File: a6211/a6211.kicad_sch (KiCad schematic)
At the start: 27 parts, among them J1 Conn_01x02, J2 Conn_01x02, J3 Conn_01x07, J4 Conn_01x05, J5 Conn_01x02, U1 A6211

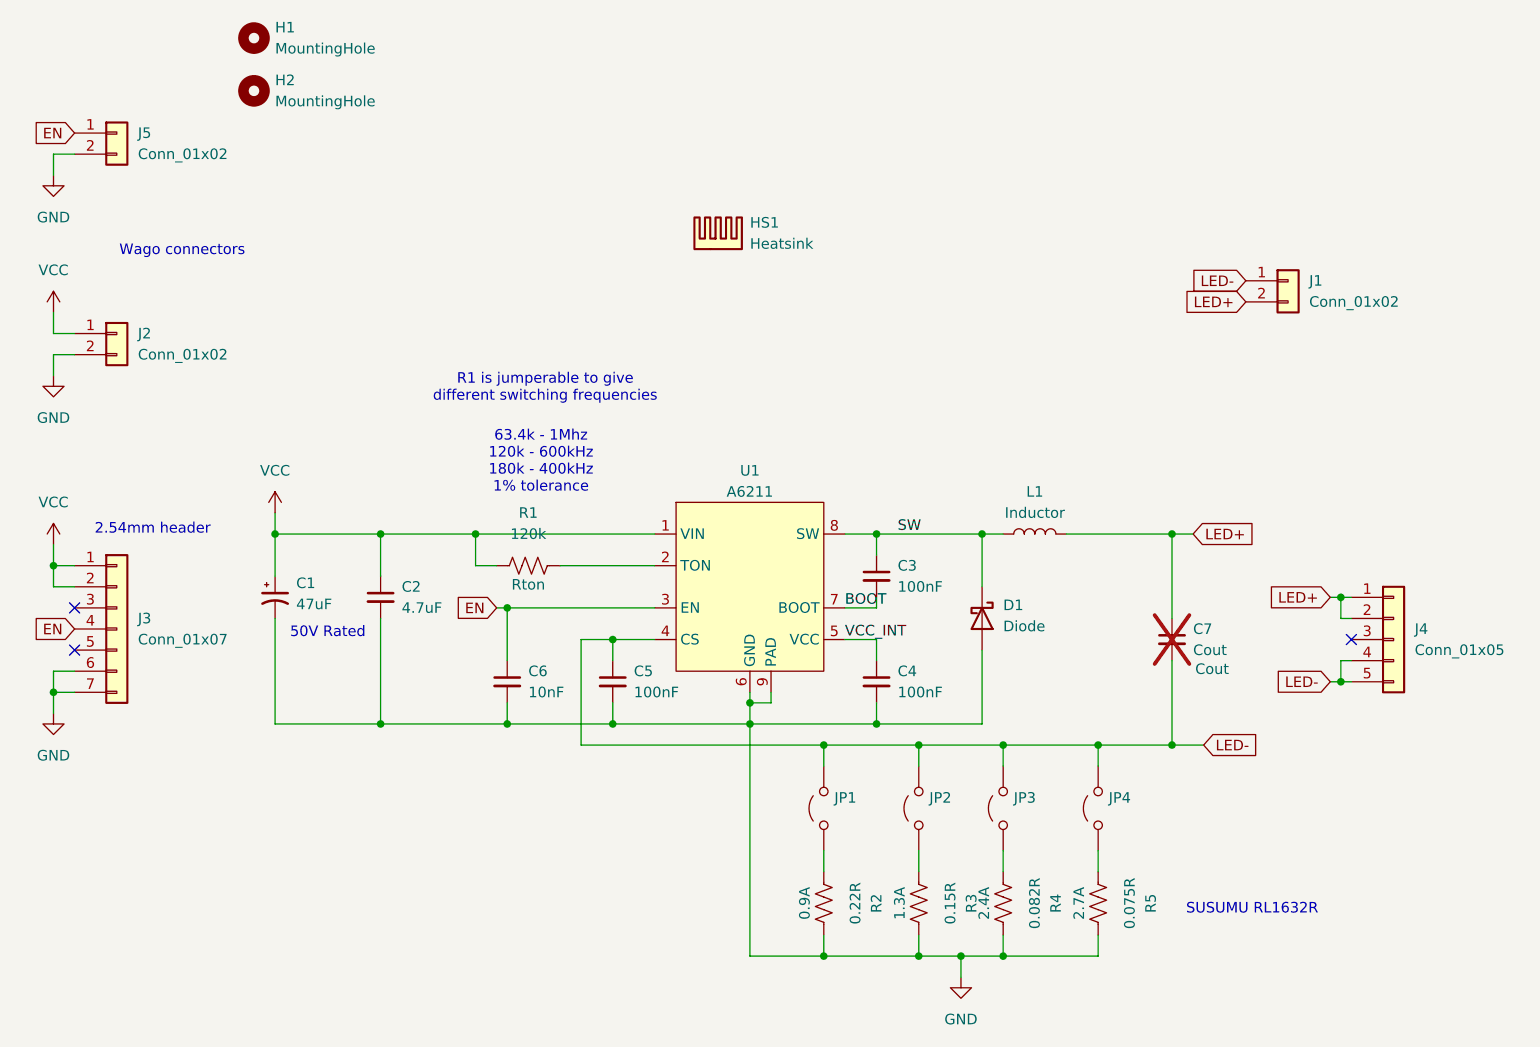
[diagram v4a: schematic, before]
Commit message: A6211 JLCPCB reference
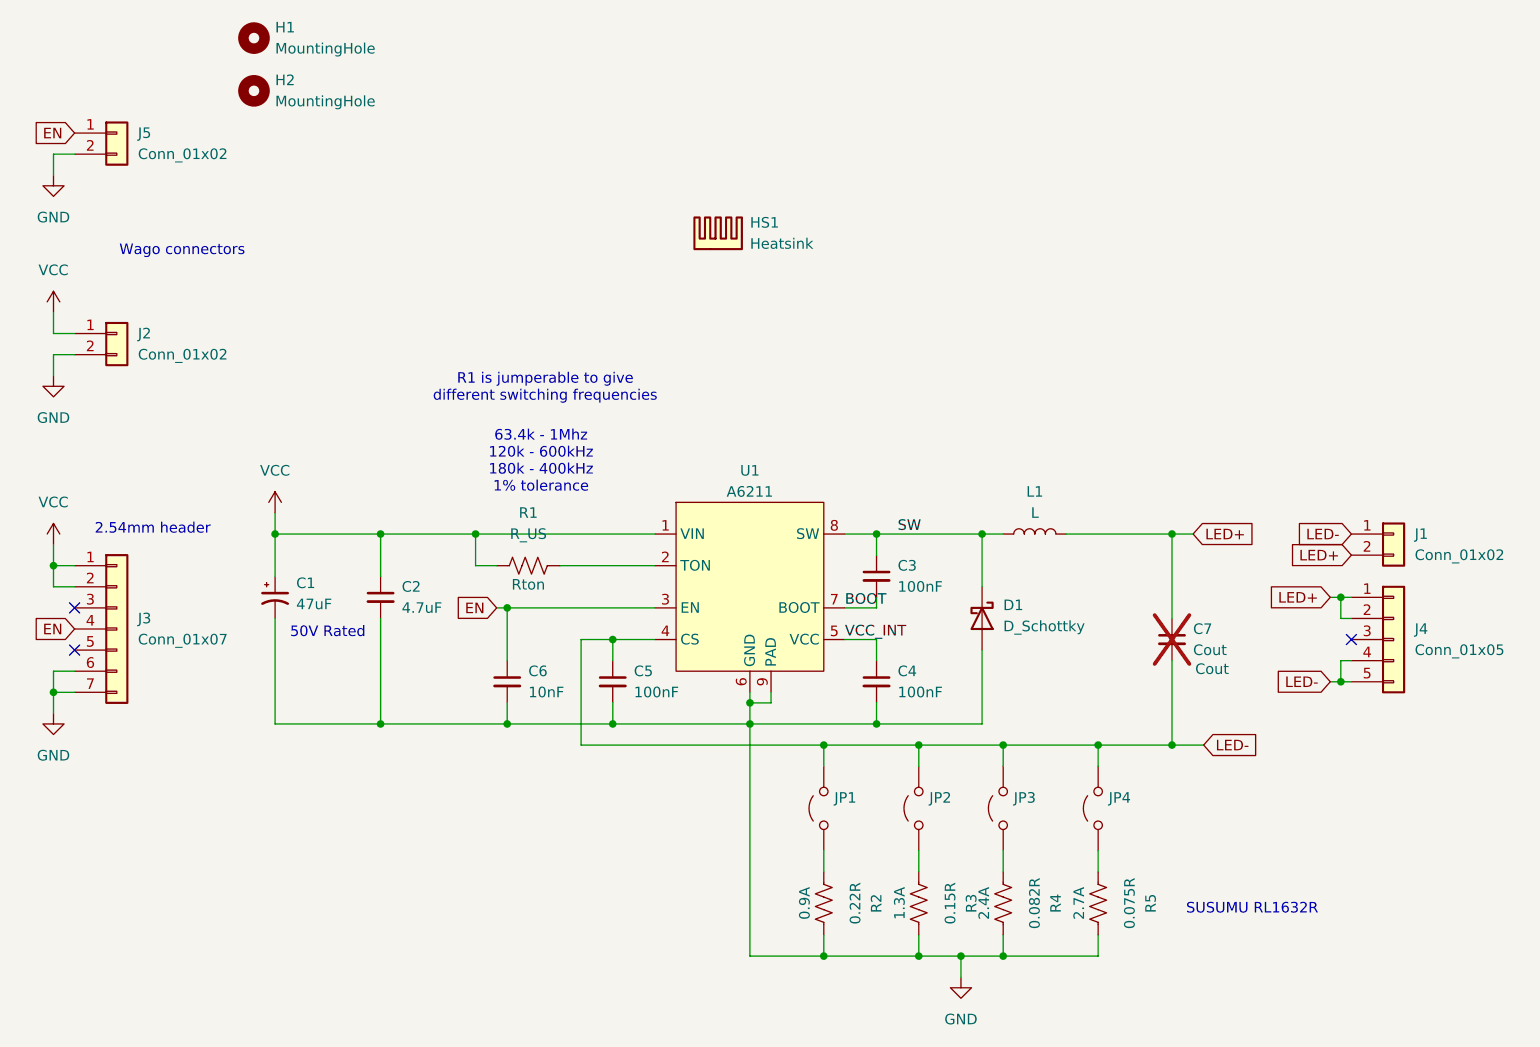
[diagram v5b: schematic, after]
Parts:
- D1: value Diode -> D_Schottky
- L1: value Inductor -> L
- R1: value 120k -> R_US
- U1: LCSC (none) -> C150827
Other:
- moved on the sheet: J1
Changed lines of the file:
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@@
 	(global_label "LED-"
 		(shape input)
-		(at 181.61 57.15 180)
+		(at 194.31 87.63 180)
 		(fields_autoplaced yes)
 		(effects
@@
 		)
 		(property "Intersheetrefs" "${INTERSHEET_REFS}"
-			(at 173.6053 57.15 0)
+			(at 186.3053 87.63 0)
 			(effects
 				(font
@@
 	(global_label "LED+"
 		(shape input)
-		(at 181.61 59.69 180)
+		(at 194.31 90.17 180)
 		(fields_autoplaced yes)
 		(effects
@@
 		)
 		(property "Intersheetrefs" "${INTERSHEET_REFS}"
-			(at 173.6053 59.69 0)
+			(at 186.3053 90.17 0)
 			(effects
 				(font
@@
 		)
 		(instances
-			(project ""
+			(project "a6211"
 				(path "/0eae7fad-4295-4de1-8a09-6528fc5757a4"
 					(reference "JP1")
@@
 			)
 		)
+		(property "LCSC" "C150827"
+			(at 121.92 93.98 0)
+			(effects
+				(font
+					(size 1.27 1.27)
+				)
+				(hide yes)
+			)
+		)
 		(pin "4"
 		)
@@
 		)
 		(instances
-			(project ""
+			(project "a6211"
 				(path "/0eae7fad-4295-4de1-8a09-6528fc5757a4"
 					(reference "U1")
@@
 		)
 		(instances
-			(project ""
+			(project "a6211"
 				(path "/0eae7fad-4295-4de1-8a09-6528fc5757a4"
 					(reference "#PWR02")
@@
 		)
 		(instances
-			(project ""
+			(project "a6211"
 				(path "/0eae7fad-4295-4de1-8a09-6528fc5757a4"
 					(reference "C1")
@@
 		)
 		(instances
-			(project ""
+			(project "a6211"
 				(path "/0eae7fad-4295-4de1-8a09-6528fc5757a4"
 					(reference "J2")
@@
 		)
 		(instances
-			(project ""
+			(project "a6211"
 				(path "/0eae7fad-4295-4de1-8a09-6528fc5757a4"
 					(reference "J3")
@@
 		)
 		(instances
-			(project ""
+			(project "a6211"
 				(path "/0eae7fad-4295-4de1-8a09-6528fc5757a4"
 					(reference "H1")
@@
 			)
 		)
-		(property "Value" "Inductor"
+		(property "Value" "L"
 			(at 156.21 85.09 90)
 			(effects
@@
 		)
 		(instances
-			(project ""
+			(project "a6211"
 				(path "/0eae7fad-4295-4de1-8a09-6528fc5757a4"
 					(reference "L1")
@@
 			)
 		)
-		(property "Value" "120k"
+		(property "Value" "R_US"
 			(at 95.25 87.63 90)
 			(effects
@@
 		)
 		(instances
-			(project ""
+			(project "a6211"
 				(path "/0eae7fad-4295-4de1-8a09-6528fc5757a4"
 					(reference "R1")
@@
 	(symbol
 		(lib_id "Connector_Generic:Conn_01x02")
-		(at 186.69 57.15 0)
+		(at 199.39 87.63 0)
 		(unit 1)
 		(exclude_from_sim no)
@@
 		(fields_autoplaced yes)
 		(property "Reference" "J1"
-			(at 189.23 57.1499 0)
+			(at 201.93 87.6299 0)
 			(effects
 				(font
@@
 		)
 		(property "Value" "Conn_01x02"
-			(at 189.23 59.6899 0)
+			(at 201.93 90.1699 0)
 			(effects
 				(font
@@
 		)
 		(property "Footprint" "MHCI:2060-452-998-404 Wago"
-			(at 186.69 57.15 0)
+			(at 199.39 87.63 0)
 			(effects
 				(font
@@
 		)
 		(property "Datasheet" "~"
-			(at 186.69 57.15 0)
+			(at 199.39 87.63 0)
 			(effects
 				(font
@@
 		)
 		(property "Description" "Generic connector, single row, 01x02, script generated (kicad-library-utils/schlib/autogen/connector/)"
-			(at 186.69 57.15 0)
+			(at 199.39 87.63 0)
 			(effects
 				(font
@@
 		)
 		(property "MFR" "2060-452/998-404"
-			(at 186.69 57.15 0)
+			(at 199.39 87.63 0)
 			(effects
 				(font
@@
 		)
 		(instances
-			(project ""
+			(project "a6211"
 				(path "/0eae7fad-4295-4de1-8a09-6528fc5757a4"
 					(reference "J1")
@@
 		)
 		(instances
-			(project ""
+			(project "a6211"
 				(path "/0eae7fad-4295-4de1-8a09-6528fc5757a4"
 					(reference "J4")
@@
 		)
 		(instances
-			(project ""
+			(project "a6211"
 				(path "/0eae7fad-4295-4de1-8a09-6528fc5757a4"
 					(reference "C7")
@@
 		)
 		(instances
-			(project ""
+			(project "a6211"
 				(path "/0eae7fad-4295-4de1-8a09-6528fc5757a4"
 					(reference "HS1")
@@
 			)
 		)
-		(property "Value" "Diode"
+		(property "Value" "D_Schottky"
 			(at 152.4 98.7424 90)
 			(effects
@@
 		)
 		(instances
-			(project ""
+			(project "a6211"
 				(path "/0eae7fad-4295-4de1-8a09-6528fc5757a4"
 					(reference "D1")

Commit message: A6211 v1.1
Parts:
- removed JP1, JP2, JP3, JP4: ~, Jumper:SolderJumper-2_P1.3mm_Open_RoundedPad1.0x1.5mm, symbol Jumper:Jumper_2_Open
- removed R4: 0.082R, Resistor_SMD:R_1206_3216Metric, symbol Device:R_US
- removed R5: 0.075R, Resistor_SMD:R_1206_3216Metric, symbol Device:R_US
- added C8: 470nF, Capacitor_SMD:C_1206_3216Metric, symbol Device:C_Small
- added JP1: Jumper_3_Open, Jumper:SolderJumper-3_P1.3mm_Open_RoundedPad1.0x1.5mm_NumberLabels, symbol Jumper:Jumper_3_Open
- C1: LCSC (none) -> C40078
- C2: LCSC (none) -> C29823
- C3: value 100nF -> 47nF; LCSC (none) -> C1622
- C4, C5: LCSC (none) -> C14663
- C6: LCSC (none) -> C57112
- C7: value Cout -> 2.2uF; footprint Capacitor_SMD:C_0603_1608Metric_Pad1.08x0.95mm_HandSolder -> Capacitor_SMD:C_1206_3216Metric; LCSC (none) -> C50254; now fitted
- D1: LCSC (none) -> C7436542; MFR B560C-13-F -> (none)
- L1: value L -> 10uH; footprint Inductor_SMD:L_10.4x10.4_H4.8 -> Inductor_SMD:L_Coilcraft_XAL6060-XXX; LCSC (none) -> C5119929; MFR B82464G4103M -> (none)
- R1: LCSC (none) -> C23231; now not fitted; now left out of the parts list
- R2: value 0.22R -> 120k; footprint Resistor_SMD:R_1206_3216Metric -> Resistor_SMD:R_0603_1608Metric_Pad0.98x0.95mm_HandSolder; LCSC (none) -> C25808; MFR RL1632R-R220-F -> (none)
- R3: LCSC (none) -> C2683383
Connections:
- net GND: no longer R2.2
- net LED+: now also C8.1
- net LED-: now also R3.1, JP1.2 (C); no longer C7.2
- net VCC: now also R2.1; no longer R1.1
- net at R1.2: no longer U1.2 (TON)
- new net: R2.2, U1.2 (TON)
- new net: C7.2, JP1.3 (B)
- new net: C8.2, JP1.1 (A)

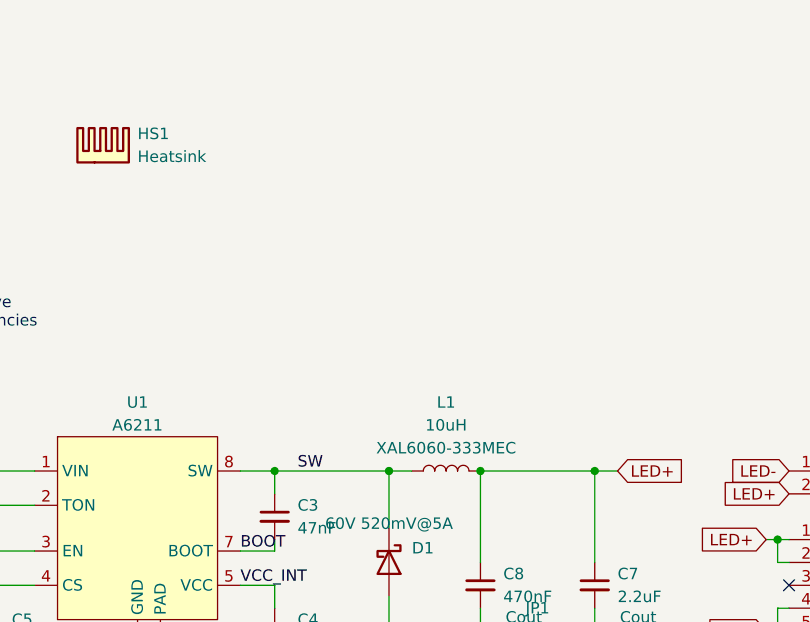
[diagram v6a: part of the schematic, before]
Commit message: A6211 - cheaper inductor
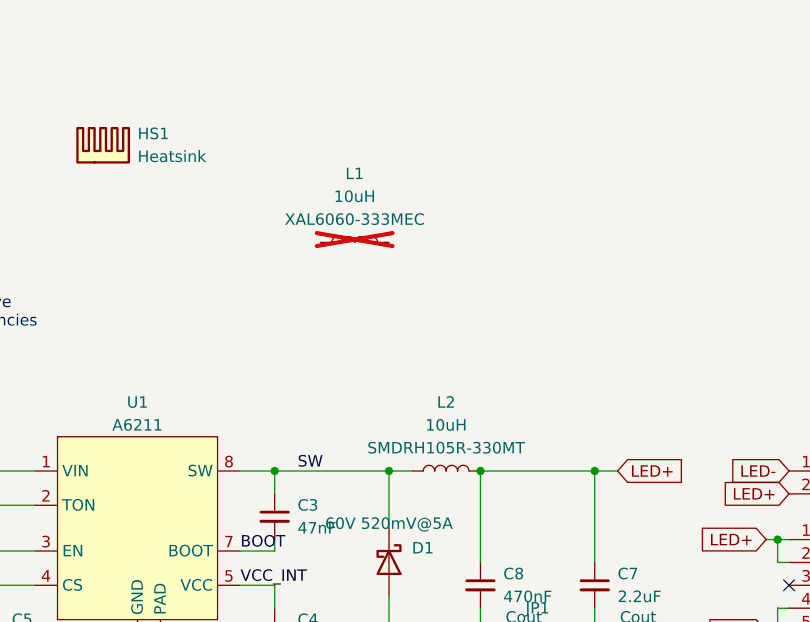
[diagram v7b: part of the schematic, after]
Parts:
- added L2: 10uH, Inductor_SMD:L_10.4x10.4_H4.8, symbol Device:L
- C8: footprint Capacitor_SMD:C_1206_3216Metric -> Capacitor_SMD:C_0805_2012Metric; LCSC C50254 -> C13967
- L1: now not fitted; now left out of the parts list
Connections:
- net LED+: now also L2.2; no longer L1.2
- net SW: now also L2.1; no longer L1.1
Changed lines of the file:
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@@
 	)
 	(junction
-		(at 160.02 87.63)
-		(diameter 0)
-		(color 0 0 0 0)
-	)
-	(junction
 		(at 121.92 110.49)
 		(diameter 0)
@@
 	)
 	(junction
+		(at 160.02 87.63)
+		(diameter 0)
+		(color 0 0 0 0)
+	)
+	(junction
 		(at 166.37 113.03)
 		(diameter 0)
@@
 	)
 	(symbol
+		(lib_id "Device:L")
+		(at 156.21 87.63 90)
+		(unit 1)
+		(exclude_from_sim no)
+		(in_bom yes)
+		(on_board yes)
+		(dnp no)
+		(fields_autoplaced yes)
+		(property "Reference" "L2"
+			(at 156.21 80.01 90)
+			(effects
+				(font
+					(size 1.27 1.27)
+				)
+			)
+		)
+		(property "Value" "10uH"
+			(at 156.21 82.55 90)
+			(effects
+				(font
+					(size 1.27 1.27)
+				)
+			)
+		)
+		(property "Footprint" "Inductor_SMD:L_10.4x10.4_H4.8"
+			(at 156.21 87.63 0)
+			(effects
+				(font
+					(size 1.27 1.27)
+				)
+				(hide yes)
+			)
+		)
+		(property "Datasheet" "~"
+			(at 156.21 87.63 0)
+			(effects
+				(font
+					(size 1.27 1.27)
+				)
+				(hide yes)
+			)
+		)
+		(property "Description" "SMDRH105R-330MT"
+			(at 156.21 85.09 90)
+			(effects
+				(font
+					(size 1.27 1.27)
+				)
+			)
+		)
+		(property "LCSC" "C9186"
+			(at 156.21 87.63 90)
+			(effects
+				(font
+					(size 1.27 1.27)
+				)
+				(hide yes)
+			)
+		)
+		(pin "1"
+		)
+		(pin "2"
+		)
+		(instances
+			(project "a6211"
+				(path "/0eae7fad-4295-4de1-8a09-6528fc5757a4"
+					(reference "L2")
+					(unit 1)
+				)
+			)
+		)
+	)
+	(symbol
 		(lib_id "A6211:A6211")
 		(at 121.92 93.98 0)
@@
 			)
 		)
-		(property "Footprint" "Capacitor_SMD:C_1206_3216Metric"
+		(property "Footprint" "Capacitor_SMD:C_0805_2012Metric"
 			(at 160.02 100.33 0)
 			(effects
@@
 			)
 		)
-		(property "LCSC" "C50254"
+		(property "LCSC" "C13967"
 			(at 160.02 100.33 0)
 			(effects
@@
 	)
 	(symbol
-		(lib_id "power:GND")
-		(at 38.1 44.45 0)
+		(lib_id "Device:L")
+		(at 146.05 62.23 90)
 		(unit 1)
-		(exclude_from_sim no)
-		(in_bom yes)
-		(on_board yes)
-		(dnp no)
+		(exclude_from_sim yes)
+		(in_bom no)
+		(on_board no)
+		(dnp yes)
 		(fields_autoplaced yes)
-		(property "Reference" "#PWR07"
-			(at 38.1 50.8 0)
+		(property "Reference" "L1"
+			(at 146.05 54.61 90)
 			(effects
 				(font
 					(size 1.27 1.27)
 				)
-				(hide yes)
 			)
 		)
-		(property "Value" "GND"
-			(at 38.1 49.53 0)
+		(property "Value" "10uH"
+			(at 146.05 57.15 90)
 			(effects
 				(font
@@
 			)
 		)
-		(property "Footprint" ""
-			(at 38.1 44.45 0)
+		(property "Footprint" "Inductor_SMD:L_Coilcraft_XAL6060-XXX"
+			(at 146.05 62.23 0)
 			(effects
 				(font
@@
 			)
 		)
-		(property "Datasheet" ""
-			(at 38.1 44.45 0)
+		(property "Datasheet" "~"
+			(at 146.05 62.23 0)
 			(effects
 				(font
@@
 			)
 		)
-		(property "Description" "Power symbol creates a global label with name \"GND\" , ground"
-			(at 38.1 44.45 0)
+		(property "Description" "XAL6060-333MEC"
+			(at 146.05 59.69 90)
+			(effects
+				(font
+					(size 1.27 1.27)
+				)
+			)
+		)
+		(property "LCSC" "C5119929"
+			(at 146.05 62.23 90)
 			(effects
 				(font
@@
 		(pin "1"
 		)
+		(pin "2"
+		)
 		(instances
 			(project "a6211"
 				(path "/0eae7fad-4295-4de1-8a09-6528fc5757a4"
-					(reference "#PWR07")
+					(reference "L1")
 					(unit 1)
 				)
@@
 	)
 	(symbol
-		(lib_id "Device:R_US")
-		(at 95.25 91.44 90)
+		(lib_id "power:GND")
+		(at 38.1 44.45 0)
 		(unit 1)
 		(exclude_from_sim no)
@@
 		(on_board yes)
 		(dnp no)
-		(property "Reference" "R2"
-			(at 95.25 85.09 90)
+		(fields_autoplaced yes)
+		(property "Reference" "#PWR07"
+			(at 38.1 50.8 0)
 			(effects
 				(font
 					(size 1.27 1.27)
 				)
+				(hide yes)
 			)
 		)
-		(property "Value" "120k"
-			(at 95.25 87.63 90)
+		(property "Value" "GND"
+			(at 38.1 49.53 0)
 			(effects
 				(font
@@
 			)
 		)
-		(property "Footprint" "Resistor_SMD:R_0603_1608Metric_Pad0.98x0.95mm_HandSolder"
-			(at 95.504 90.424 90)
+		(property "Footprint" ""
+			(at 38.1 44.45 0)
 			(effects
 				(font
@@
 			)
 		)
-		(property "Datasheet" "~"
-			(at 95.25 91.44 0)
+		(property "Datasheet" ""
+			(at 38.1 44.45 0)
 			(effects
 				(font
@@
 			)
 		)
-		(property "Description" "Rton"
-			(at 95.25 93.726 90)
-			(effects
-				(font
-					(size 1.27 1.27)
-				)
-			)
-		)
-		(property "LCSC" "C25808"
-			(at 95.25 91.44 90)
+		(property "Description" "Power symbol creates a global label with name \"GND\" , ground"
+			(at 38.1 44.45 0)
 			(effects
 				(font
@@
 			)
 		)
-		(pin "2"
-		)
 		(pin "1"
 		)
@@
 			(project "a6211"
 				(path "/0eae7fad-4295-4de1-8a09-6528fc5757a4"
-					(reference "R2")
+					(reference "#PWR07")
 					(unit 1)
 				)
@@
 	)
 	(symbol
-		(lib_id "Device:L")
-		(at 156.21 87.63 90)
+		(lib_id "Device:R_US")
+		(at 95.25 91.44 90)
 		(unit 1)
 		(exclude_from_sim no)
@@
 		(on_board yes)
 		(dnp no)
-		(fields_autoplaced yes)
-		(property "Reference" "L1"
-			(at 156.21 80.01 90)
+		(property "Reference" "R2"
+			(at 95.25 85.09 90)
 			(effects
 				(font
@@
 			)
 		)
-		(property "Value" "10uH"
-			(at 156.21 82.55 90)
+		(property "Value" "120k"
+			(at 95.25 87.63 90)
 			(effects
 				(font
@@
 			)
 		)
-		(property "Footprint" "Inductor_SMD:L_Coilcraft_XAL6060-XXX"
-			(at 156.21 87.63 0)
+		(property "Footprint" "Resistor_SMD:R_0603_1608Metric_Pad0.98x0.95mm_HandSolder"
+			(at 95.504 90.424 90)
 			(effects
 				(font
@@
 		)
 		(property "Datasheet" "~"
-			(at 156.21 87.63 0)
+			(at 95.25 91.44 0)
 			(effects
 				(font
@@
 			)
 		)
-		(property "Description" "XAL6060-333MEC"
-			(at 156.21 85.09 90)
+		(property "Description" "Rton"
+			(at 95.25 93.726 90)
 			(effects
 				(font
@@
 			)
 		)
-		(property "LCSC" "C5119929"
-			(at 156.21 87.63 90)
+		(property "LCSC" "C25808"
+			(at 95.25 91.44 90)
 			(effects
 				(font
@@
 			)
 		)
-		(pin "1"
-		)
 		(pin "2"
 		)
+		(pin "1"
+		)
 		(instances
 			(project "a6211"
 				(path "/0eae7fad-4295-4de1-8a09-6528fc5757a4"
-					(reference "L1")
+					(reference "R2")
 					(unit 1)
 				)

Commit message: A6211 v1.1
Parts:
- removed C7: 2.2uF, Capacitor_SMD:C_1206_3216Metric, symbol Device:C_Small
- removed C8: 470nF, Capacitor_SMD:C_0805_2012Metric, symbol Device:C_Small
- removed JP1: Jumper_3_Open, Jumper:SolderJumper-3_P1.3mm_Open_RoundedPad1.0x1.5mm_NumberLabels, symbol Jumper:Jumper_3_Open
- C3: value 47nF -> 100nF; LCSC C1622 -> C14663
